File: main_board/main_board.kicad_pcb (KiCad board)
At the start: 2 copper layers, 80 x 80 mm, 115 parts, among them J10 B5B-XH, J11 B5B-XH, J12 B3B-XH, J13 B5B-XH, J2 Conn_01x02, J3 Conn_01x02, J4 EncSide, J5 MainSide, J6 EncSide, J7 MainSide, J8 Conn_01x02, J9 Conn_01x02, Q1 ST-1KL3A, Q10 DTC114E, Q2 ST-1KL3A, Q3 ST-1KL3A, Q4 ST-1KL3A, Q5 IRLML6344, Q6 IRLML6344, Q7 IRLML6344, Q8 IRLML6344, Q9 DTC114E, U1 ADCS7476, U10 AS5047D, U11 LSM6DSR, U12 OKL-T/6-W12N-C, U13 XC6221B332MR, U14 FT232RL, U15 SL2.1A, U2 BD63573NUV, U3 ADCS7476, U4 ADCS7476, U5 BD63573NUV, U6 ESP32-S3-PICO-1-N8R2, U7 AS5047D, U8 ADCS7476, U9 ADCS7476, Y1 12MHz

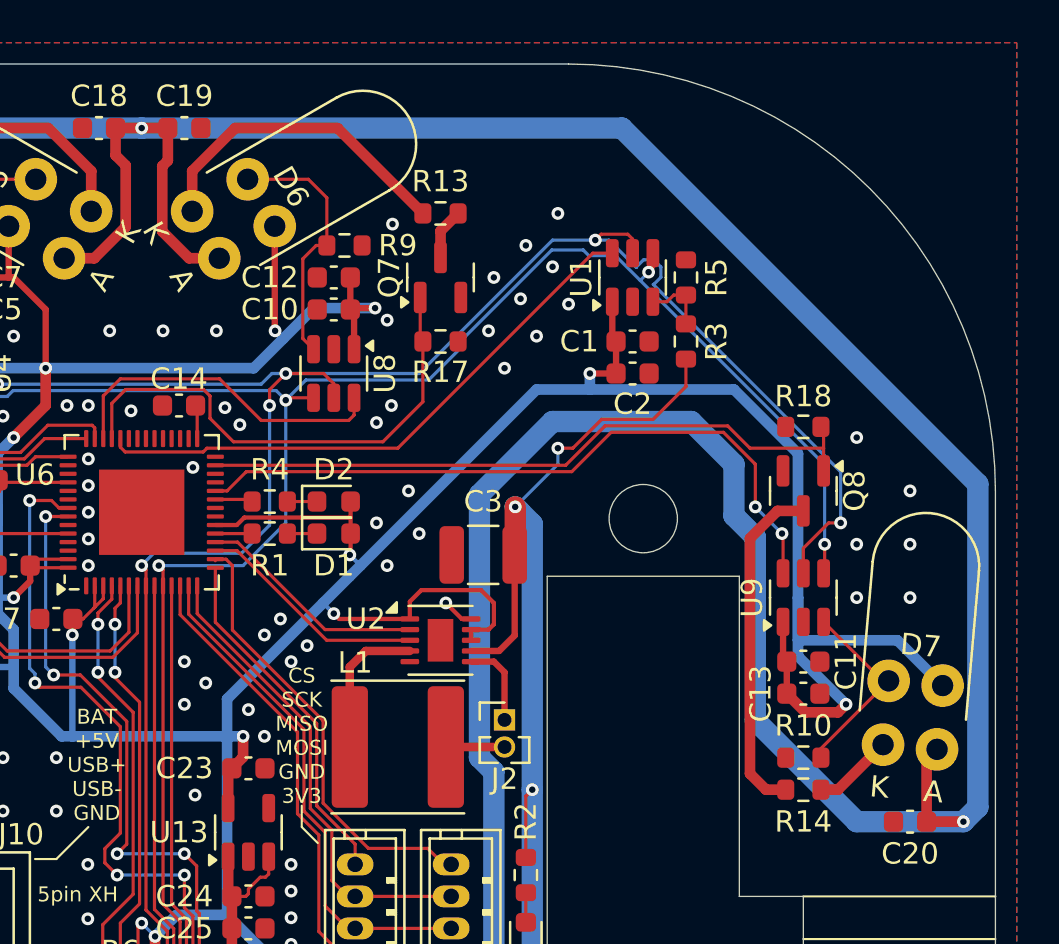
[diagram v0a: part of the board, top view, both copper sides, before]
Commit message: 充電回路追加
Signed-off-by: Kazuki Iida <elkel53930@gmail.com>
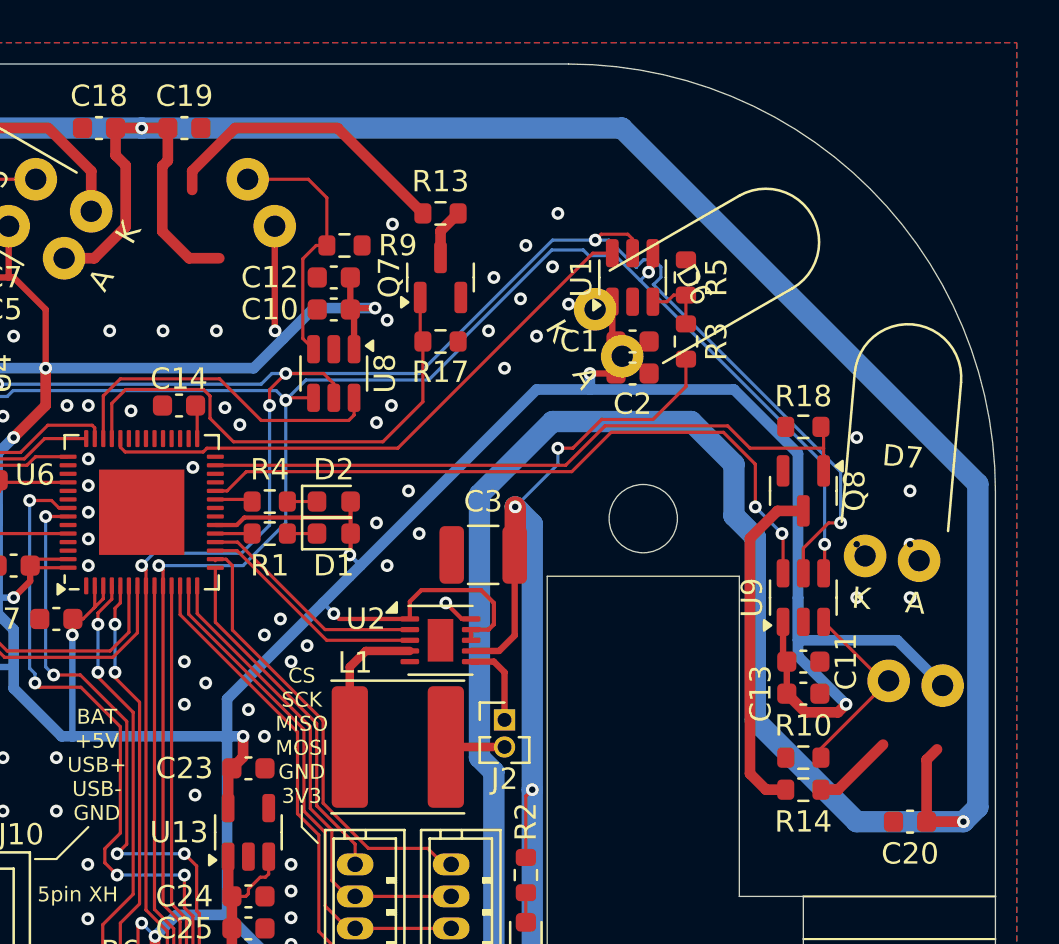
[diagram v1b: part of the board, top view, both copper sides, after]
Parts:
- moved D6 19.4 mm to (205.9, 52.6)
- moved D7 8.88 mm to (219.2, 63.2)
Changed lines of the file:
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@@
 	(footprint "Library:SFH4550"
 		(layer "F.Cu")
-		(at 187 48 -60)
+		(at 205.879392 52.592332 -60)
 		(property "Reference" "D6"
 			(at 0.051443 -4.589102 300)
@@
 	(footprint "Library:SFH4550"
 		(layer "F.Cu")
-		(at 220 72 -5)
+		(at 219.159465 63.158484 -5)
 		(property "Reference" "D7"
 			(at 0.084108 -4.775503 355)
@@
 		(min_thickness 0.2)
 		(filled_areas_thickness no)
-		(fill yes
+		(fill
 			(thermal_gap 0.2)
 			(thermal_bridge_width 0.3)

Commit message: アートワーク開始
Signed-off-by: Kazuki Iida <elkel53930@gmail.com>
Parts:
- removed C18, C19: 1608 6.3V 10uF, Capacitor_SMD:C_0603_1608Metric
- removed D6, D7: SFH4550, Library:SFH4550
- removed G***: LOGO, Library:AMacLogo
- removed H11: M2 mounting hole, MountingHole:MountingHole_2.2mm_M2
- removed Q10, Q9: DTC114E, Package_TO_SOT_SMD:SOT-723
- removed Y1: 12MHz, Crystal:Crystal_HC49-4H_Vertical
- added BT1: 1000mAh LiPo 2S, Library:Battery_Connector, F.Cu at (146.5, 139.2)
- added C38: CC0603KRX7R9BB104, Capacitor_SMD:C_0603_1608Metric, F.Cu at (200.8, 62.2)
- added C39: CC0603KRX7R9BB104, Capacitor_SMD:C_0603_1608Metric, F.Cu at (197.5, 55.8)
- added C40: CC0603KRX7R9BB104, Capacitor_SMD:C_0603_1608Metric, F.Cu at (201.0, 55.8)
- added C41: CC0603KRX7R9BB104, Capacitor_SMD:C_0603_1608Metric, F.Cu at (199.5, 64.5)
- added H5: M2 mounting hole, MountingHole:MountingHole_2.2mm_M2, F.Cu at (25.6, 27.2)
- added H9: M2 mounting hole, MountingHole:MountingHole_2.2mm_M2, F.Cu at (37.5, 27.2)
- added J1: Conn_01x02, Connector_PinHeader_1.27mm:PinHeader_1x02_P1.27mm_Vertical, F.Cu at (179.0, 86.0)
- added J16: B4B-ZR(LF)(SN), Connector_JST:JST_ZH_B4B-ZR_1x04_P1.50mm_Vertical, F.Cu at (198.5, 70.0)
- added R22: 0603WAF1001T5E, Resistor_SMD:R_0603_1608Metric, F.Cu at (152.0, 130.8)
- added SW1: SS-22SBH2, Library:SS-22SBH2, F.Cu at (125.5, 151.2)
- added U16: LM74700QDBVRQ1, Package_TO_SOT_SMD:SOT-23-6, F.Cu at (150.0, 116.0)
- added U17: FT231XQ-R, Package_DFN_QFN:QFN-20-1EP_4x4mm_P0.5mm_EP2.5x2.5mm, F.Cu at (195.5, 62.0)
- C1, C11, C15, C16, C21, C22, C4, C5: value 1608 50V 0.1uF -> CC0603KRX7R9BB104
- C10: value 1608 50V 0.1uF -> CL21A106KAYNNNE; footprint Capacitor_SMD:C_0603_1608Metric -> Capacitor_SMD:C_0805_2012Metric
- C12: value 1608 25V 1uF -> CC0603KRX7R9BB104
- C13, C2, C6, C7: value 1608 25V 1uF -> CL10A105KB8NNNC
- C14: value 1608 50V 0.1uF -> CL10A105KB8NNNC
- C17, C20: value 1608 6.3V 10uF -> CL10A106KP8NNNC
- C23, C24, C25, C8: value 1608 6.3V 10uF -> CC0603KRX7R9BB104
- C26: value 1608 6.3V 10uF -> CL21A106KAYNNNE; footprint Capacitor_SMD:C_0603_1608Metric -> Capacitor_SMD:C_0805_2012Metric
- C27: value CL31A226KAHNNNE -> CL21A106KAYNNNE; footprint Capacitor_SMD:C_1206_3216Metric -> Capacitor_SMD:C_0805_2012Metric
- C28, C29: value CL31A106KBHNNNE -> CL10A106KP8NNNC; footprint Capacitor_SMD:C_1206_3216Metric -> Capacitor_SMD:C_0603_1608Metric
- C3, C9: value 3225 3.3u 16V -> CL21A106KAYNNNE; footprint Capacitor_SMD:C_1210_3225Metric -> Capacitor_SMD:C_0805_2012Metric
- C30: value 0.1u 1608 -> CL10A106KP8NNNC
- C31: value 1608 0.1u -> CL10A106KP8NNNC
- C32: value 0.1u 1608 -> CL21A106KAYNNNE; footprint Capacitor_SMD:C_0603_1608Metric -> Capacitor_SMD:C_0805_2012Metric
- C33: value 1608 0.1u -> CC0603KRX7R9BB104
- C34, C35: value 10uF -> CC0603KRX7R9BB104; footprint Capacitor_SMD:C_0805_2012Metric -> Capacitor_SMD:C_0603_1608Metric
- C36, C37: value 1608 6.3V 10uF -> CL10A105KB8NNNC
- D1, D2: value 1608 LED -> D-060306G1/SS2/G1
- D3: value 1608 R LED -> KT-0603R
- D4: value SFH4550 -> 1N5819WS; footprint Library:SFH4550_Mirror -> Diode_SMD:D_SOD-323
- D5: value SFH4550 -> KT-0603R; footprint Library:SFH4550_Mirror -> LED_SMD:LED_0603_1608Metric
- H1, H2, H3: value M3 mounting hole -> M2.6 mounting hole; footprint MountingHole:MountingHole_3.2mm_M3 -> Library:M2.6 Mounting Hole
- H4: value M2 mounting hole -> M2.6 mounting hole; footprint MountingHole:MountingHole_2.2mm_M2 -> Library:M2.6 Mounting Hole
- J10: value B5B-XH -> Conn_01x02; footprint Connector_JST:JST_XH_B5B-XH-A_1x05_P2.50mm_Vertical -> Connector_PinHeader_2.54mm:PinHeader_1x02_P2.54mm_Vertical
- J11, J13: value B5B-XH -> B2B-XH-A(LF)(SN); footprint Connector_JST:JST_XH_B5B-XH-A_1x05_P2.50mm_Vertical -> Connector_PinHeader_2.54mm:PinHeader_1x02_P2.54mm_Vertical
- J12: value B3B-XH -> B2B-XH-A(LF)(SN); footprint Connector_JST:JST_XH_B3B-XH-A_1x03_P2.50mm_Vertical -> Connector_PinHeader_2.54mm:PinHeader_1x02_P2.54mm_Vertical
- J3: value Conn_01x02 -> 2.54mm PinHeader; footprint Connector_PinHeader_1.27mm:PinHeader_1x02_P1.27mm_Vertical -> Connector_PinHeader_2.54mm:PinHeader_2x05_P2.54mm_Vertical
- J5: value MainSide -> B6B-ZR
- J6: value EncSide -> 2.54mm PinHeader; footprint Library:EncoderPad -> Connector_PinHeader_2.54mm:PinHeader_2x05_P2.54mm_Vertical
- J7: value MainSide -> EncSide; footprint Connector_JST:JST_ZH_B6B-ZR_1x06_P1.50mm_Vertical -> Library:EncoderPad
- J8: value Conn_01x02 -> B6B-ZR; footprint Library:PowerCable -> Connector_JST:JST_ZH_B6B-ZR_1x06_P1.50mm_Vertical
- J9: value Conn_01x02 -> MJ-179PH; footprint Connector_PinHeader_2.54mm:PinHeader_1x02_P2.54mm_Vertical -> Library:PJ-002A
- Q1, Q2: value ST-1KL3A -> IRLML6344; footprint Library:ST-1KL3A_Mirror -> Package_TO_SOT_SMD:SOT-23; moved to F.Cu
- Q3, Q4: value ST-1KL3A -> IRLML6344; footprint Library:ST-1KL3A -> Package_TO_SOT_SMD:SOT-23; moved to F.Cu
- Q5, Q6: value IRLML6344 -> DMT6008LFG; footprint Package_TO_SOT_SMD:SOT-23 -> Package_SON:Diodes_PowerDI3333-8
- Q7, Q8: value IRLML6344 -> DTC114E; footprint Package_TO_SOT_SMD:SOT-23 -> Package_TO_SOT_SMD:SOT-723
- R1: value 1608 1k -> 0603WAF1002T5E
- R10, R7, R8, R9: value 1608 470.5% -> 0603WAF4700T5E
- R11, R12, R13: value 1608 470 -> 0603WAF4700T5E
- R14: value 1608 470 -> 0603WAF1002T5E
- R15, R16, R17, R2: value 1608 10k -> 0603WAF1002T5E
- R18, R3, R5: value 1608 10k -> 0603WAF1001T5E
- R19: value 0603WAF1001T5E -> 0603WAF3300T5E
- R20: value 0603WAF1001T5E -> 0603WAF100JT5E
- R4: value 1608 1k -> 0603WAF1001T5E
- R6: value 1608 10k -> 0603WAF4700T5E
- U14: value FT232RL -> LM74700QDBVRQ1; footprint Package_SO:SSOP-28_5.3x10.2mm_P0.65mm -> Package_TO_SOT_SMD:SOT-23-6
- U15: value SL2.1A -> MCP73213T-A6SI/MF; footprint Package_SO:SOP-16_3.9x9.9mm_P1.27mm -> Package_DFN_QFN:DFN-10-1EP_3x3mm_P0.5mm_EP1.58x2.35mm
- U6: value ESP32-S3-PICO-1-N8R2 -> ESP32-S3-WROOM-1; footprint Package_DFN_QFN:QFN-56-1EP_7x7mm_P0.4mm_EP4x4mm -> RF_Module:ESP32-S3-WROOM-1
- U7: value AS5047D -> ADCS7476; footprint Package_SO:TSSOP-14_4.4x5mm_P0.65mm -> Package_TO_SOT_SMD:SOT-23-6
- U9: value ADCS7476 -> AS5047D; footprint Package_TO_SOT_SMD:SOT-23-6 -> Package_SO:TSSOP-14_4.4x5mm_P0.65mm
- moved H6 202.8 mm to (25.6, 33.2)
- moved H7 193.3 mm to (31.6, 27.2)
- moved J4 176.5 mm to (53.3, 40.5), turned to 0 degrees
- moved C15 155.0 mm to (62.0, 101.5), turned to 0 degrees
- moved J7 150.7 mm to (53.3, 44.4), turned to 0 degrees
- moved U9 147.2 mm to (72.1, 100.5), turned to 0 degrees
- moved H8 129.9 mm to (31.6, 33.2)
- moved H10 119.0 mm to (37.5, 33.2)
- moved H3 96.7 mm to (137.5, 128.0)
- moved D5 95.2 mm to (164.8, 141.8), turned to -90 degrees
- moved R14 91.4 mm to (129.0, 43.0)
- moved C16 90.7 mm to (62.0, 104.0), turned to 0 degrees
- moved R10 88.9 mm to (129.0, 50.0)
- moved R18 83.9 mm to (182.8, 134.5), turned to 90 degrees
- moved D3 82.3 mm to (131.5, 38.5), turned to 180 degrees
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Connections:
- C10 pad 1: +3V3 -> GND
- C10 pad 2: GND -> +BATT
- C12 pad 1: GND -> +3V3
- C12 pad 2: +3V3 -> GND
- C14 pad 1: Net-(U6-VDD_SPI) -> GND
- C14 pad 2: GND -> +3V3
- C15 pad 1: Net-(J4-Pin_1) -> Net-(J4-Pin_2)
- C15 pad 2: Net-(J4-Pin_2) -> Net-(J4-Pin_1)
- C16 pad 1: Net-(J6-Pin_1) -> Net-(J7-Pin_2)
- C16 pad 2: Net-(J6-Pin_2) -> Net-(J7-Pin_1)
- C20 pad 2: +5V -> +3V3
- C21 pad 1: +3V3 -> GND
- C21 pad 2: GND -> +3V3
- C22 pad 1: +3V3 -> GND
- C22 pad 2: GND -> +3V3
- C23 pad 1: +3V3 -> GND
- C23 pad 2: GND -> /Power/EXT_PWR
- C24 pad 1: GND -> Net-(U14-VCAP)
- C24 pad 2: +5V -> /Power/EXT_PWR
- C25 pad 2: +5V -> +BATT
- C26 pad 2: +5V -> +BATT
- C27 pad 1: GND -> +5V
- C27 pad 2: +BATT -> GND
- C3 pad 1: +BATT -> GND
- C3 pad 2: GND -> +BATT
- C30 pad 1: +5V -> GND
- C30 pad 2: GND -> +5V
- C31 pad 1: CHIP_PU -> GND
- C31 pad 2: GND -> +3V3
- C32 pad 1: Net-(U14-3V3OUT) -> +5V
- C33 pad 1: GPIO0 -> GND
- C33 pad 2: GND -> Net-(BT1-+)
- C34 pad 1: Net-(U15-VDD33) -> Net-(U16-VCAP)
- C34 pad 2: GND -> Net-(BT1-+)
- C35 pad 1: Net-(U15-VDD18) -> GND
- C35 pad 2: GND -> +BATT
- C36 pad 2: +3V3 -> /Power/EXT_PWR
- C37 pad 2: +3V3 -> Net-(BT1-+)
- C9 pad 1: +BATT -> GND
- C9 pad 2: GND -> +3V3
- D1 pad 1: Net-(D1-K) -> GND
- D1 pad 2: +3V3 -> Net-(D1-A)
- D3 pad 1: GND -> Net-(D3-K)
- D3 pad 2: Net-(D3-A) -> +3V3
- D4 pad 1: Net-(D4-K) -> +BATT
- D5 pad 2: +5V -> /Power/EXT_PWR
- J10 pad 1: GND -> +5V
- J10 pad 2: /Power/DM2 -> GND
- J11 pad 1: GND -> +BATT
- J11 pad 2: /Power/DM3 -> GND
- J12 pad 1: GND -> +BATT
- J12 pad 2: /Power/USB+ -> GND
- J13 pad 1: GND -> +BATT
- J13 pad 2: /Power/DM4 -> GND
- J3 pad 1: Net-(J3-Pin_1) -> /LS_LED
- J3 pad 2: Net-(J3-Pin_2) -> /LS_PHTR
- J6 pad 1: Net-(J6-Pin_1) -> /RS_PHTR
- J6 pad 2: Net-(J6-Pin_2) -> /RS_LED
- J6 pad 3: Net-(J6-Pin_3) -> /RF_PHTR
- J6 pad 4: Net-(J6-Pin_4) -> /RF_LED
- J6 pad 5: Net-(J6-Pin_5) -> unconnected-(J6-Pin_5-Pad5)
- J6 pad 6: Net-(J6-Pin_6) -> unconnected-(J6-Pin_6-Pad6)
- J7 pad 1: +3V3 -> Net-(J7-Pin_1)
- J7 pad 2: GND -> Net-(J7-Pin_2)
- J7 pad 3: /SPI1_MOSI -> Net-(J7-Pin_3)
- J7 pad 4: /SPI1_MISO -> Net-(J7-Pin_4)
- J7 pad 5: /SPI1_SCK -> Net-(J7-Pin_5)
- J7 pad 6: /CS_ENC_R -> Net-(J7-Pin_6)
- J8 pad 1: GND -> +3V3
- J8 pad 2: +BATT -> GND
- J9 pad 1: GND -> /Power/EXT_PWR
- J9 pad 2: +5V -> GND
- L1 pad 2: Net-(J2-Pin_2) -> Net-(J1-Pin_2)
- L2 pad 2: Net-(J3-Pin_2) -> Net-(J2-Pin_2)
- Q1 pad 1: +3V3 -> /LF_EN
- Q1 pad 2: Net-(Q1-E) -> GND
- Q2 pad 1: +3V3 -> /LS_EN
- Q2 pad 2: Net-(Q2-E) -> GND
- Q3 pad 1: +3V3 -> /RS_EN
- Q3 pad 2: Net-(Q3-E) -> GND
- Q4 pad 1: +3V3 -> /RF_EN
- Q4 pad 2: Net-(Q4-E) -> GND
- Q5 pad 1: /LF_EN -> /Power/EXT_PWR
- Q5 pad 2: GND -> /Power/EXT_PWR
- Q5 pad 3: Net-(Q5-D) -> /Power/EXT_PWR
- Q6 pad 1: /LS_EN -> Net-(BT1-+)
- Q6 pad 2: GND -> Net-(BT1-+)
- Q6 pad 3: Net-(Q6-D) -> Net-(BT1-+)
- Q7 pad 1: /RS_EN -> /Power/DTR
- Q7 pad 2: GND -> /Power/RTS
- Q7 pad 3: Net-(Q7-D) -> CHIP_PU
- Q8 pad 1: /RF_EN -> /Power/RTS
- Q8 pad 2: GND -> /Power/DTR
- Q8 pad 3: Net-(Q8-D) -> GPIO0
- R1 pad 1: /LED_0 -> Net-(D1-A)
- R1 pad 2: Net-(D1-K) -> +BATT
- R10 pad 1: Net-(Q4-E) -> Net-(Q1-D)
- R10 pad 2: GND -> /LF_LED
- R11 pad 1: Net-(Q5-D) -> Net-(Q2-D)
- R11 pad 2: Net-(D4-K) -> /LS_LED
- R12 pad 1: Net-(Q6-D) -> Net-(Q3-D)
- R12 pad 2: Net-(D5-K) -> /RS_LED
- R13 pad 1: Net-(Q7-D) -> Net-(Q4-D)
- R13 pad 2: Net-(D6-K) -> /RF_LED
- R14 pad 1: Net-(Q8-D) -> GND
- R14 pad 2: Net-(D7-K) -> /LF_EN
- R15 pad 2: /LF_EN -> /LS_EN
- R16 pad 2: /LS_EN -> /RS_EN
- R17 pad 2: /RS_EN -> /RF_EN
- R18 pad 1: GND -> Net-(U12-Trim)
- R18 pad 2: /RF_EN -> Net-(R18-Pad2)
- R19 pad 1: Net-(U12-Trim) -> Net-(R18-Pad2)
- R2 pad 1: Net-(D3-A) -> Net-(U1-VIN)
- R20 pad 2: Net-(R20-Pad2) -> GND
- R21 pad 1: Net-(R20-Pad2) -> Net-(U15-STAT)
- R21 pad 2: GND -> Net-(D5-K)
- R3 pad 2: +BATT -> GND
- R4 pad 1: Net-(D2-K) -> /LED_0
- R4 pad 2: /LED_1 -> Net-(D2-K)
- R5 pad 1: GND -> /LED_1
- R5 pad 2: Net-(U1-VIN) -> Net-(D3-K)
- R6 pad 1: CHIP_PU -> GND
- R6 pad 2: +3V3 -> /LF_PHTR
- R7 pad 1: Net-(Q1-E) -> GND
- R7 pad 2: GND -> /LS_PHTR
- R8 pad 1: Net-(Q2-E) -> GND
- R8 pad 2: GND -> /RS_PHTR
- R9 pad 1: Net-(Q3-E) -> GND
- R9 pad 2: GND -> /RF_PHTR
- U1 pad 6: /CS_BATT -> /BATT_CS
- U10 pad 1: Net-(J6-Pin_6) -> Net-(J7-Pin_6)
- U10 pad 12: Net-(J6-Pin_1) -> Net-(J7-Pin_1)
- U10 pad 13: Net-(J6-Pin_2) -> Net-(J7-Pin_2)
- U10 pad 2: Net-(J6-Pin_5) -> Net-(J7-Pin_5)
- U10 pad 3: Net-(J6-Pin_4) -> Net-(J7-Pin_4)
- U10 pad 4: Net-(J6-Pin_3) -> Net-(J7-Pin_3)
- U10 pad 5: Net-(J6-Pin_2) -> Net-(J7-Pin_2)
- U14 pad 1: RXD0 -> Net-(U14-VCAP)
- U14 pad 2: /Power/DTR -> GND
- U14 pad 3: /Power/RTS -> Net-(U14-EN)
- U14 pad 4: +3V3 -> +BATT
- U14 pad 5: TXD0 -> Net-(Q5-G)
- U14 pad 6: unconnected-(U14-RI-Pad6) -> /Power/EXT_PWR
- U15 pad 1: /Power/DM4 -> /Power/EXT_PWR
- U15 pad 10: /Power/USB+ -> Net-(U15-PROG)
- U15 pad 11: +5V -> GND
- U15 pad 2: /Power/DP4 -> /Power/EXT_PWR
- U15 pad 3: /Power/DM3 -> Net-(BT1-+)
- U15 pad 4: /Power/DP3 -> Net-(BT1-+)
- U15 pad 5: /Power/DM2 -> unconnected-(U15-NC-Pad5)
- U15 pad 6: /Power/DP2 -> unconnected-(U15-NC-Pad6)
- U15 pad 7: /Power/DM1 -> Net-(U15-STAT)
- U15 pad 8: /Power/DP1 -> GND
- U15 pad 9: /Power/USB- -> GND
- U2 pad 6: Net-(J2-Pin_1) -> Net-(J1-Pin_1)
- U3 pad 3: Net-(Q1-E) -> /LF_PHTR
- U3 pad 6: /CS_LF -> /LF_CS
- U4 pad 3: Net-(Q2-E) -> /LS_PHTR
- U4 pad 6: /CS_LS -> /LS_CS
- U5 pad 6: Net-(J3-Pin_1) -> Net-(J2-Pin_1)
- U6 pad 1: unconnected-(U6-LNA_IN-Pad1) -> GND
- U6 pad 10: /SPI2_SCK -> /SPI1_MOSI
- U6 pad 11: /CS_IMU -> /SPI1_MISO
- U6 pad 12: /SPI1_MOSI -> /SPI1_SCK
- U6 pad 13: /SPI1_MISO -> /CS_ENC_L
- U6 pad 14: /SPI1_SCK -> /CS_ENC_R
- U6 pad 15: /CS_ENC_L -> /PWM_L
- U6 pad 16: /CS_ENC_R -> /CWCCW_L
- U6 pad 17: /PWM_R -> /SPI2_MISO
- U6 pad 18: /CWCCW_R -> /SPI2_MOSI
- U6 pad 19: /LED_0 -> /SPI2_SCK
- U6 pad 20: +3V3 -> /CS_IMU
- U6 pad 23: /LED_1 -> unconnected-(U6-IO21-Pad23)
- U6 pad 24: /CS_RF -> /PWM_R
- U6 pad 25: unconnected-(U6-GPIO19-Pad25) -> /CWCCW_R
- U6 pad 27: /RF_EN -> GPIO0
- U6 pad 29: Net-(U6-VDD_SPI) -> unconnected-(U6-IO36-Pad29)
- U6 pad 3: +3V3 -> CHIP_PU
- U6 pad 33: unconnected-(U6-SPICLK-Pad33) -> /RF_CS
- U6 pad 34: unconnected-(U6-SPIQ-Pad34) -> /RS_CS
- U6 pad 35: unconnected-(U6-SPID-Pad35) -> /RS_EN
- U6 pad 36: unconnected-(U6-SPICLK_N-Pad36) -> RXD0
- U6 pad 37: unconnected-(U6-SPICLK_P-Pad37) -> TXD0
- U6 pad 38: /CS_BATT -> /RF_EN
- U6 pad 39: /RS_EN -> /BATT_CS
- U6 pad 4: CHIP_PU -> /LED_0
- U6 pad 40: /CS_RS -> unconnected-(U6-GND-Pad40)
- U6 pad 41: /CS_LS -> unconnected-(U6-GND-Pad41)
- U6 pad 5: GPIO0 -> /LED_1
- U6 pad 6: /PWM_L -> /LF_EN
- U6 pad 7: /CWCCW_L -> /LS_EN
- U6 pad 8: /SPI2_MISO -> /LS_CS
- U6 pad 9: /SPI2_MOSI -> /LF_CS
- U7 pad 1: Net-(J4-Pin_6) -> +3V3
- U7 pad 2: Net-(J4-Pin_5) -> GND
- U7 pad 3: Net-(J4-Pin_4) -> /RS_PHTR
- U7 pad 4: Net-(J4-Pin_3) -> /SPI2_SCK
- U7 pad 5: Net-(J4-Pin_2) -> /SPI2_MISO
- U7 pad 6: unconnected-(U7-B-Pad6) -> /RS_CS
- U8 pad 3: Net-(Q3-E) -> /RF_PHTR
- U8 pad 6: /CS_RS -> /RF_CS
- U9 pad 1: +3V3 -> Net-(J4-Pin_6)
- U9 pad 2: GND -> Net-(J4-Pin_5)
- U9 pad 3: Net-(Q4-E) -> Net-(J4-Pin_4)
- U9 pad 4: /SPI2_SCK -> Net-(J4-Pin_3)
- U9 pad 5: /SPI2_MISO -> Net-(J4-Pin_2)
- U9 pad 6: /CS_RF -> unconnected-(U9-B-Pad6)
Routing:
- net +5V: track 366.3 -> 2.64 mm, vias 11 -> 0
- net +3V3: track 310.6 -> 7.28 mm, vias 19 -> 1
- net +BATT: track 206.7 -> 68.0 mm, vias 4 -> 0
- net CHIP_PU: track 22.8 -> 99.9 mm
- net GPIO0: track 24.5 -> 78.0 mm, vias 2 -> 0
- net /CS_LF: track 38.1 -> 0.00 mm
- net GND: track 33.4 -> 0.00 mm, vias 146 -> 0
- net /CS_RF: track 32.7 -> 0.00 mm, vias 2 -> 0
- net /Power/DP3: track 32.5 -> 0.00 mm
- net /Power/DM3: track 31.7 -> 0.00 mm
- net /CS_BATT: track 27.4 -> 0.00 mm
- net /SPI2_MISO: track 140.9 -> 114.5 mm, vias 7 -> 6
- net Net-(J4-Pin_1): track 25.8 -> 0.00 mm
- net /CWCCW_R: track 10.8 -> 35.3 mm, vias 0 -> 2
- net /Power/DP2: track 23.9 -> 0.00 mm
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- added copper zone on F.Cu, net +BATT
- added copper zone on F.Cu, net /Power/EXT_PWR
- added copper zone on F.Cu, net Net-(BT1-+)
- added copper zone on F.Cu, net Net-(J1-Pin_1)
- added copper zone on F.Cu, net Net-(J2-Pin_1)
- removed copper zone on B.Cu, net GND
- removed copper zone on F.Cu, net GND
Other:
- board size 80 x 80 mm -> 84 x 114 mm
- board text removed: "+5V"
- board text removed: "3pin XH"
- board text removed: "5pin XH"
- board text removed: "BAT +5V USB+ USB- GND"
- board text removed: "BATT 2S 6-8.4V"
- board text removed: "CS SCK MISO MOSI GND 3V3"
- board text removed: "GND"
- board text removed: "TWILIGHT Main Board v1.0"
- board text removed: "ToRPi"
- board text removed: "USB- USB+ GND"

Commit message: アートワークひととおり完成
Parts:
- removed J13: B2B-XH-A(LF)(SN), Connector_PinHeader_2.54mm:PinHeader_1x02_P2.54mm_Vertical
- added C18: CC0603KRX7R9BB104, Capacitor_SMD:C_0603_1608Metric, F.Cu at (152.4, 80.7)
- added C19: CC0603KRX7R9BB104, Capacitor_SMD:C_0603_1608Metric, F.Cu at (173.6, 84.8)
- added G***: LOGO, Library:AMacLogo, F.Cu at (126.1, 71.4)
- J10, J11, J12: footprint Connector_PinHeader_2.54mm:PinHeader_1x02_P2.54mm_Vertical -> Connector_JST:JST_XH_B2B-XH-AM_1x02_P2.50mm_Vertical
- moved SW1 34.3 mm to (126.0, 117.0), turned to -90 degrees
- moved C28 11.4 mm to (176.5, 97.5)
- moved C29 11.4 mm to (176.5, 99.5)
- moved C30 11.4 mm to (176.5, 101.5)
- moved C31 11.4 mm to (176.5, 90.5)
- moved U13 11.4 mm to (176.5, 94.0)
- moved J11 7.25 mm to (127.8, 133.2)
- moved R18 2.61 mm to (182.0, 137.0)
- moved R19 2.61 mm to (185.0, 137.0)
- moved R20 2.61 mm to (188.0, 137.0)
- moved J12 1.06 mm to (127.8, 126.0)
- moved C3 1.03 mm to (152.4, 82.5), turned to 180 degrees
- moved D1 1.00 mm to (181.5, 141.5)
- moved R6 1.00 mm to (145.5, 50.0)
- moved R7 1.00 mm to (139.0, 50.0)
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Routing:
- net +3V3: track 7.28 -> 283.1 mm, vias 1 -> 12
- net +5V: track 2.64 -> 88.5 mm, vias 0 -> 3
- net +BATT: track 68.0 -> 148.5 mm
- net GND: track 0.00 -> 51.7 mm, vias 0 -> 128
- net /Power/EXT_PWR: track 19.3 -> 61.5 mm, vias 0 -> 1
- net Net-(U14-EN): track 0.00 -> 41.2 mm, vias 0 -> 1
- net Net-(U16-EN): track 0.00 -> 28.1 mm, vias 0 -> 1
- net Net-(BT1-+): track 0.00 -> 26.6 mm, vias 0 -> 1
- net /RF_PHTR: track 0.00 -> 10.3 mm
- net /RF_LED: track 0.00 -> 9.89 mm
- net /RS_PHTR: track 0.00 -> 9.51 mm
- net /RS_LED: track 0.00 -> 5.92 mm
- net Net-(U1-VIN): track 0.00 -> 5.89 mm
- net GPIO0: track 78.0 -> 72.5 mm
- net Net-(Q4-D): track 0.00 -> 3.40 mm
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- added copper zone on F.Cu, net +5V
- added copper zone on B.Cu, net GND
- added copper zone on F.Cu, net GND
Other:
- outline, holes or cut-outs redrawn
- board text added: "TWILIGHT"

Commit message: アートワーク微修正
Signed-off-by: Kazuki Iida <elkel53930@gmail.com>
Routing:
- net GND: vias 128 -> 138
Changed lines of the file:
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@@
 		(tags "SOT TO_SOT_SMD")
 		(property "Reference" "U13"
-			(at 0 -2.4 90)
+			(at 0 -3 180)
 			(layer "F.SilkS")
 			(effects
@@
 		(tags "capacitor")
 		(property "Reference" "C22"
-			(at 0 -1.43 0)
+			(at 0 1.5 0)
 			(layer "F.SilkS")
 			(effects
@@
 	)
 	(via
+		(at 163 125)
+		(size 0.6)
+		(drill 0.3)
+		(layers "F.Cu" "B.Cu")
+		(free yes)
+		(net 3)
+	)
+	(via
 		(at 162 52)
 		(size 0.6)
@@
 	)
 	(via
+		(at 152.5 113)
+		(size 0.6)
+		(drill 0.3)
+		(layers "F.Cu" "B.Cu")
+		(free yes)
+		(net 3)
+	)
+	(via
 		(at 167.5 92.5)
 		(size 0.6)
@@
 	)
 	(via
+		(at 150.5 64)
+		(size 0.6)
+		(drill 0.3)
+		(layers "F.Cu" "B.Cu")
+		(free yes)
+		(net 3)
+	)
+	(via
 		(at 165 49)
 		(size 0.6)
@@
 	)
 	(via
+		(at 147.5 67)
+		(size 0.6)
+		(drill 0.3)
+		(layers "F.Cu" "B.Cu")
+		(free yes)
+		(net 3)
+	)
+	(via
 		(at 165 37.5)
 		(size 0.6)
@@
 	)
 	(via
+		(at 163 120)
+		(size 0.6)
+		(drill 0.3)
+		(layers "F.Cu" "B.Cu")
+		(free yes)
+		(net 3)
+	)
+	(via
 		(at 135 49.5)
 		(size 0.6)
@@
 	)
 	(via
+		(at 162.5 113)
+		(size 0.6)
+		(drill 0.3)
+		(layers "F.Cu" "B.Cu")
+		(free yes)
+		(net 3)
+	)
+	(via
 		(at 137.5 100)
 		(size 0.6)
@@
 	)
 	(via
+		(at 152 112)
+		(size 0.6)
+		(drill 0.3)
+		(layers "F.Cu" "B.Cu")
+		(free yes)
+		(net 3)
+	)
+	(via
 		(at 165 65)
 		(size 0.6)
@@
 	)
 	(via
+		(at 163 115)
+		(size 0.6)
+		(drill 0.3)
+		(layers "F.Cu" "B.Cu")
+		(free yes)
+		(net 3)
+	)
+	(via
 		(at 194.5 39)
 		(size 0.6)
@@
 	)
 	(via
+		(at 149 65.5)
+		(size 0.6)
+		(drill 0.3)
+		(layers "F.Cu" "B.Cu")
+		(free yes)
+		(net 3)
+	)
+	(via
 		(at 200 47.5)
 		(size 0.6)
@@
 	)
 	(via
+		(at 172.6 87.6)
+		(size 0.6)
+		(drill 0.3)
+		(layers "F.Cu" "B.Cu")
+		(free yes)
+		(net 3)
+	)
+	(via
 		(at 162.5 116.5)
 		(size 0.5)
@@
 	)
 	(segment
-		(start 190.2635 34.076)
-		(end 190.8 34.6125)
+		(start 188.029595 33.075)
+		(end 188.374 33.419405)
 		(width 0.15)
 		(layer "F.Cu")
@@
 	)
 	(segment
-		(start 186.75748 35.75)
-		(end 186.75748 33.515223)
+		(start 188.374 33.419405)
+		(end 188.374 33.738588)
 		(width 0.15)
 		(layer "F.Cu")
@@
 	)
 	(segment
-		(start 187.197703 33.075)
-		(end 188.029595 33.075)
+		(start 188.711412 34.076)
+		(end 190.2635 34.076)
 		(width 0.15)
 		(layer "F.Cu")
@@
 	)
 	(segment
-		(start 188.029595 33.075)
-		(end 188.374 33.419405)
+		(start 186.75748 33.515223)
+		(end 187.197703 33.075)
 		(width 0.15)
 		(layer "F.Cu")
@@
 	(segment
 		(start 170.75 39.16)
-		(end 183.34748 39.16)
+		(end 184.09374 39.16)
 		(width 0.15)
 		(layer "F.Cu")
@@
 	)
 	(segment
-		(start 188.711412 34.076)
-		(end 190.2635 34.076)
+		(start 187.197703 33.075)
+		(end 188.029595 33.075)
 		(width 0.15)
 		(layer "F.Cu")
@@
 	)
 	(segment
-		(start 186.75748 33.515223)
-		(end 187.197703 33.075)
+		(start 184.09374 39.16)
+		(end 186.75748 36.49626)
 		(width 0.15)
 		(layer "F.Cu")
@@
 	)
 	(segment
-		(start 188.374 33.419405)
-		(end 188.374 33.738588)
+		(start 186.75748 36.49626)
+		(end 186.75748 33.515223)
 		(width 0.15)
 		(layer "F.Cu")
@@
 	)
 	(segment
-		(start 183.34748 39.16)
-		(end 186.75748 35.75)
+		(start 190.2635 34.076)
+		(end 190.8 34.6125)
 		(width 0.15)
 		(layer "F.Cu")
@@
 	)
 	(segment
-		(start 174.35 89.3)
-		(end 174.375 89.275)
+		(start 173.4 89.3)
+		(end 174.35 89.3)
 		(width 0.9)
 		(layer "F.Cu")
@@
 	)
 	(segment
+		(start 167.5 89.3)
+		(end 166.6 89.3)
+		(width 0.9)
+		(layer "F.Cu")
+		(net 80)
+	)
+	(segment
 		(start 184 46.775)
 		(end 185.5 46.775)
@@
 	)
 	(segment
+		(start 174.35 89.3)
+		(end 174.375 89.275)
+		(width 0.9)
+		(layer "F.Cu")
+		(net 80)
+	)
+	(segment
 		(start 174.375 82.5)
 		(end 174.375 83.025)
@@
 	)
 	(segment
-		(start 172.1 89.3)
-		(end 174.35 89.3)
-		(width 0.9)
-		(layer "F.Cu")
-		(net 80)
-	)
-	(segment
 		(start 145.5625 80.6375)
 		(end 145.8 80.4)
@@
 	)
 	(segment
-		(start 168.3 89.3)
-		(end 166.6 89.3)
-		(width 0.9)
-		(layer "F.Cu")
-		(net 80)
-	)
-	(segment
-		(start 169.1 89.3)
-		(end 168.3 89.3)
-		(width 0.9)
-		(layer "F.Cu")
-		(net 80)
-	)
-	(segment
 		(start 140.8 64)
 		(end 140.6 63.8)
@@
 	)
 	(segment
-		(start 172.125 89.275)
-		(end 172.1 89.3)
-		(width 0.6)
-		(layer "F.Cu")
-		(net 80)
-	)
-	(segment
 		(start 174.375 82.225)
 		(end 174.375 83.025)
@@
 	)
 	(via
-		(at 173 89.3)
+		(at 174.35 89.3)
 		(size 0.6)
 		(drill 0.3)
@@
 	)
 	(via
-		(at 169.1 89.3)
+		(at 167.5 89.3)
 		(size 0.6)
 		(drill 0.3)
@@
 	)
 	(via
-		(at 172.1 89.3)
+		(at 173.4 89.3)
 		(size 0.6)
 		(drill 0.3)
@@
 	)
 	(via
-		(at 168.2 89.3)
+		(at 166.6 89.3)
 		(size 0.6)
 		(drill 0.3)
@@
 	)
 	(segment
-		(start 172.1 89.3)
-		(end 173 89.3)
+		(start 176.25 43.75)
+		(end 177.5 45)
 		(width 0.9)
 		(layer "B.Cu")
@@
 	)
 	(segment
-		(start 176.25 43.75)
-		(end 177.5 45)
+		(start 137 44.155082)
+		(end 142.655082 38.5)
 		(width 0.9)
 		(layer "B.Cu")
@@
 	)
 	(segment
-		(start 137 44.155082)
-		(end 142.655082 38.5)
+		(start 173.4 89.3)
+		(end 167.5 89.3)
 		(width 0.9)
 		(layer "B.Cu")
@@
 	)
 	(segment
-		(start 172.1 89.3)
-		(end 169.1 89.3)
-		(width 0.9)
-		(layer "B.Cu")
-		(net 80)
-	)
-	(segment
 		(start 130 43.25)
 		(end 130 40.25)
@@
 	)
 	(segment
+		(start 166.6 89.3)
+		(end 167.5 89.3)
+		(width 0.9)
+		(layer "B.Cu")
+		(net 80)
+	)
+	(segment
+		(start 173.4 89.3)
+		(end 174.35 89.3)
+		(width 0.9)
+		(layer "B.Cu")
+		(net 80)
+	)
+	(segment
 		(start 175.5 43)
 		(end 176.25 43.75)
@@
 	)
 	(segment
-		(start 168.2 89.3)
-		(end 169.1 89.3)
-		(width 0.9)
-		(layer "B.Cu")
-		(net 80)
-	)
-	(segment
 		(start 160.775 118.975)
 		(end 161.1375 118.6125)
@@
 	)
 	(segment
-		(start 147.5 67.5)
-		(end 147.5 77)
+		(start 151.25 64.25)
+		(end 148.5 67)
 		(width 0.15)
 		(layer "F.Cu")
@@
 	)
 	(segment
-		(start 146.75 77.75)
-		(end 145.45 77.75)
+		(start 148.5 76)
+		(end 146.75 77.75)
 		(width 0.15)
 		(layer "F.Cu")
@@
 	(segment
 		(start 151.25 55.25)
-		(end 151.25 63.75)
+		(end 151.25 64.25)
 		(width 0.15)
 		(layer "F.Cu")
@@
 	)
 	(segment
-		(start 147.5 77)
-		(end 146.75 77.75)
+		(start 148.5 67)
+		(end 148.5 76)
 		(width 0.15)
 		(layer "F.Cu")
@@
 	)
 	(segment
-		(start 151.25 63.75)
-		(end 147.5 67.5)
+		(start 146.75 77.75)
+		(end 145.45 77.75)
 		(width 0.15)
 		(layer "F.Cu")

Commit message: 12/18 基板発注
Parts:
- removed C15, C16: CC0603KRX7R9BB104, Capacitor_SMD:C_0603_1608Metric
- removed H10, H5, H6, H7, H8, H9: M2 mounting hole, MountingHole:MountingHole_2.2mm_M2
- removed J4, J7: EncSide, Library:EncoderPad
- removed U10, U9: AS5047D, Package_SO:TSSOP-14_4.4x5mm_P0.65mm
- C18, C19: value CC0603KRX7R9BB104 -> CL10A105KB8NNNC
- moved G*** 5.26 mm to (126.9, 66.2)
- moved R1 1.95 mm to (183.0, 141.0)
- moved D1 1.80 mm to (183.0, 142.5)
- moved D5 1.38 mm to (163.5, 141.2)
- moved R21 1.25 mm to (163.5, 137.8)
- moved C20 0.40 mm to (141.6, 63.2)
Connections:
- U2 pad 11: (no net) -> GND
- U5 pad 11: (no net) -> GND
- U6 pad 40: unconnected-(U6-GND-Pad40) -> GND
- U6 pad 41: unconnected-(U6-GND-Pad41) -> GND
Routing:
- net +BATT: track 148.5 -> 206.5 mm
- net GND: track 51.7 -> 59.4 mm, vias 138 -> 189
- net +5V: track 88.5 -> 94.4 mm
- net +3V3: track 283.1 -> 286.4 mm
- net /PWM_R: track 33.9 -> 35.9 mm
- net /CWCCW_R: track 35.3 -> 37.2 mm
- net /Power/EXT_PWR: track 61.5 -> 59.6 mm
- net Net-(J1-Pin_1): track 7.99 -> 9.46 mm
- net Net-(U15-STAT): track 20.3 -> 19.0 mm
- net GPIO0: track 72.5 -> 71.7 mm
- net CHIP_PU: track 98.4 -> 97.8 mm
- net Net-(D5-K): track 2.46 -> 1.89 mm
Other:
- outline, holes or cut-outs redrawn
